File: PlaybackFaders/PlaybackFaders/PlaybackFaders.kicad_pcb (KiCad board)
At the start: 2 copper layers, 1 part, among them U1 Pico

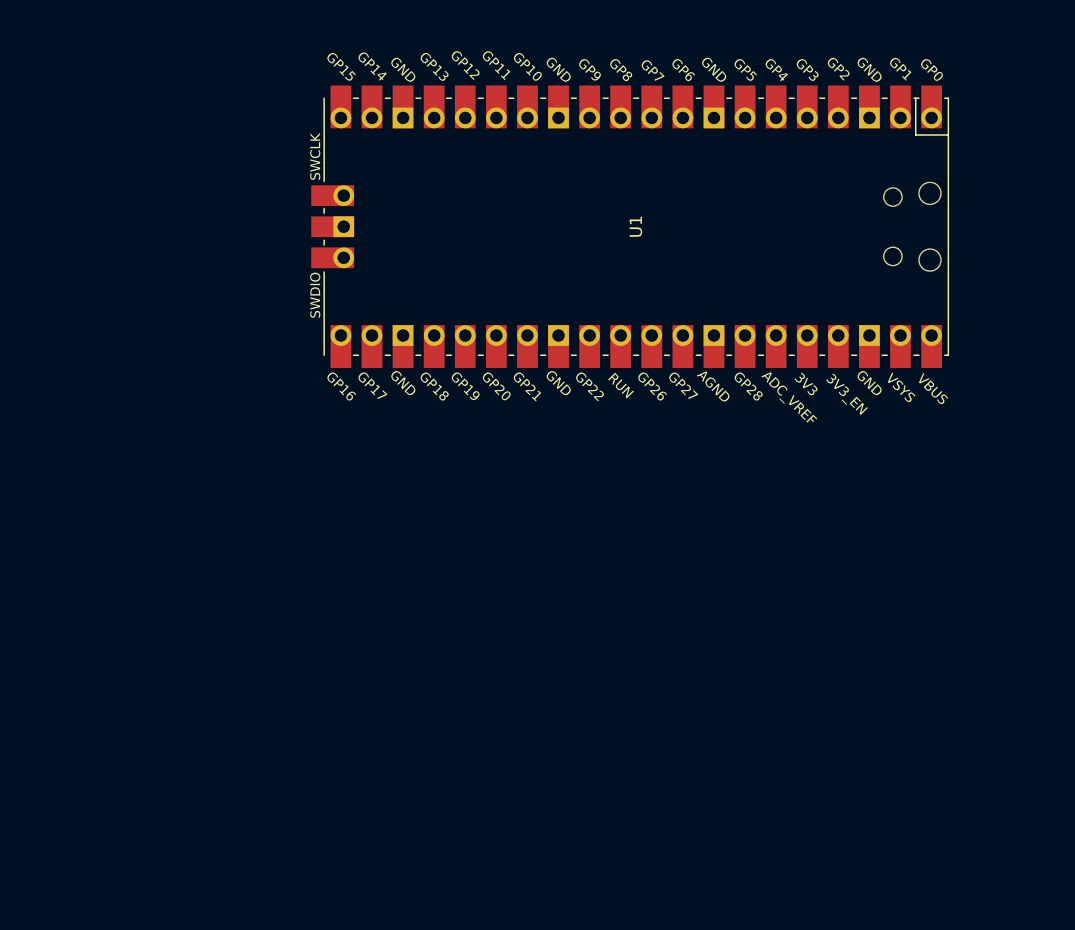
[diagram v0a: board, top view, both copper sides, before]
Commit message: CherryMX-WS2812 added with custom symbol
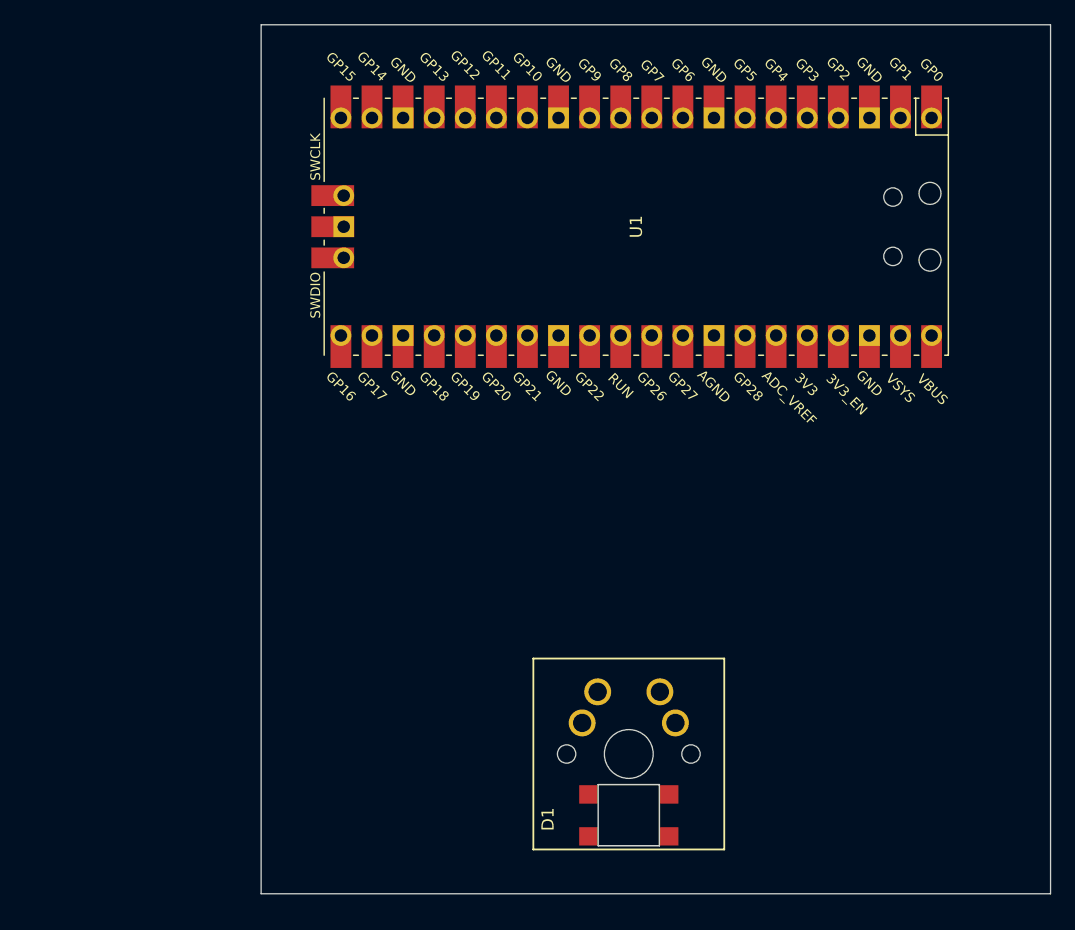
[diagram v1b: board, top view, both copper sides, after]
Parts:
- added D1: WS2812B, Cherry_MX_SK6812_BS:Cherry_MX_SK6812_BS, F.Cu at (89.0, 73.6)
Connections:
- U1 pad 23: unconnected-(U1-GND-Pad23) -> Net-(D1-VSS)
- U1 pad 28: unconnected-(U1-GND-Pad28) -> Net-(D1-Pad5)
- U1 pad 32: unconnected-(U1-GPIO27_ADC1-Pad32) -> Net-(D1-DIN)
- U1 pad 38: unconnected-(U1-GND-Pad38) -> Net-(D1-Pad6)
- U1 pad 40: unconnected-(U1-VBUS-Pad40) -> Net-(D1-VDD)
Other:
- board outline added: 64.5 x 71 mm

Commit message: Fixed CherryMX-WS2812 pin mapping
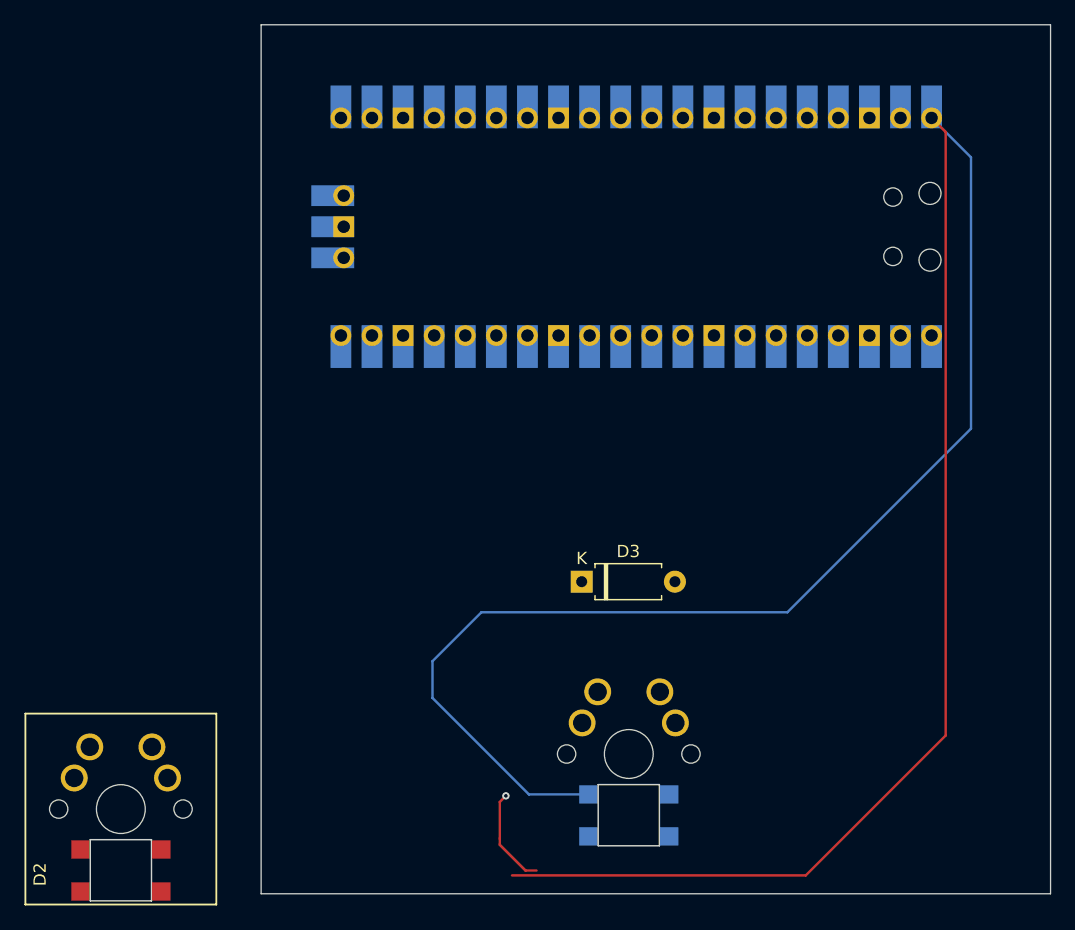
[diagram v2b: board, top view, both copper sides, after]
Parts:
- added D2: WS2812B, Cherry_MX_WS2812:Cherry_MX_SK6812_BS, F.Cu at (47.5, 78.1)
- added D3: D, Diode_THT:D_A-405_P7.62mm_Horizontal, F.Cu at (85.2, 59.5)
- D1: footprint Cherry_MX_SK6812_BS:Cherry_MX_SK6812_BS -> Cherry_MX_WS2812:Cherry_MX_SK6812_BS; moved to B.Cu
- U1: moved to B.Cu
- turned D1 to 180 degrees
- turned U1 to 90 degrees
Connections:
- D1 pad 2: unconnected-(D1-DOUT-Pad2) -> Net-(D1-DOUT)
- D1 pad 5: Net-(D1-Pad5) -> Net-(U1-GPIO22)
- U1 pad 28: Net-(D1-Pad5) -> unconnected-(U1-GND-Pad28)
- U1 pad 29: unconnected-(U1-GPIO22-Pad29) -> Net-(U1-GPIO22)
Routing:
- net Net-(D1-VDD): track 0.00 -> 188.7 mm
- net (no net): track 0.00 -> 8.08 mm, vias 0 -> 1
